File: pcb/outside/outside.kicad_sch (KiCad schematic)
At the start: 69 parts, among them J1 USB_C_Receptacle_USB2.0_16P, J2 RJ12, J3 Conn_01x08, J4 Conn_01x04, Q1 BSS138, SW1 RST, SW2 PRG, U1 ESP32-C6-MINI-1, U3 AMS1117-3.3, U4 USBLC6-2SC6, U5 USBLC6-2SC6

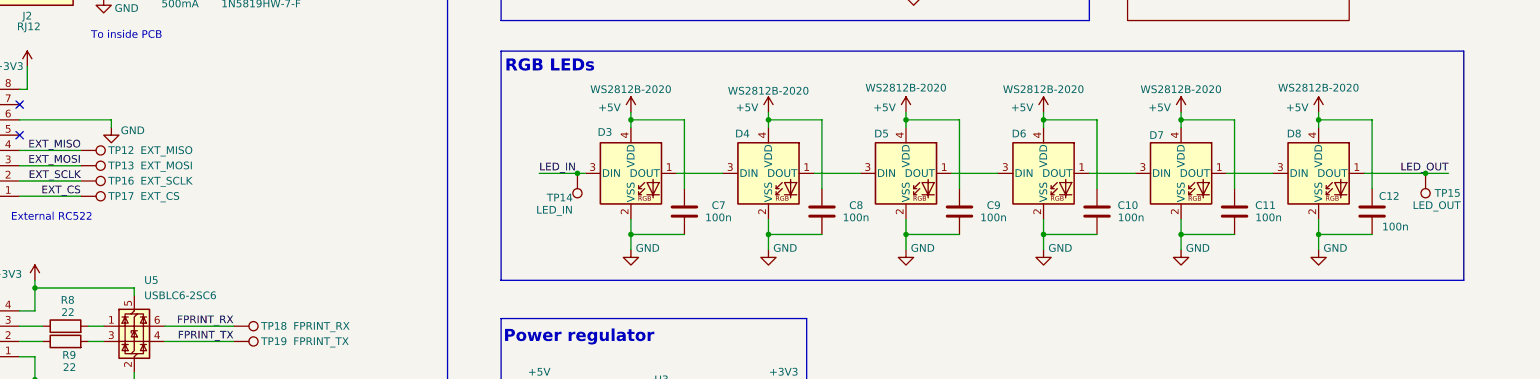
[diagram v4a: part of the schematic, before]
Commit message: fix: exclude testpoints from BOM
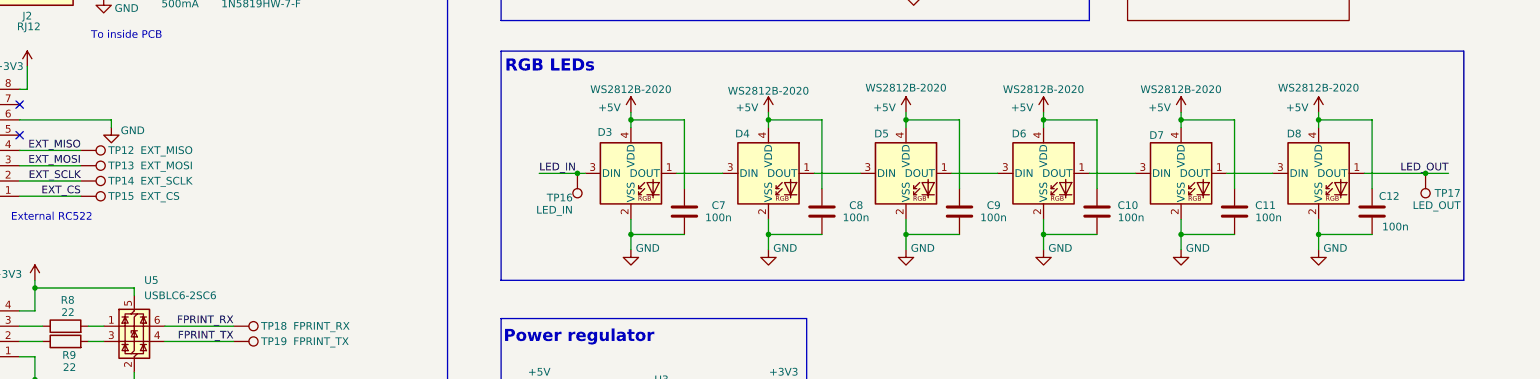
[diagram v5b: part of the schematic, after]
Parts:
- TP1, TP10, TP11, TP12, TP13, TP18, TP19, TP2, TP20, TP21, TP22, TP3, TP4, TP5, TP6, TP7, TP8, TP9: now left out of the parts list
- TP14: renamed from TP16; now left out of the parts list
- TP15: renamed from TP17; now left out of the parts list
- TP16: renamed from TP14; now left out of the parts list
- TP17: renamed from TP15; now left out of the parts list
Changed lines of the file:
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@@
 		(unit 1)
 		(exclude_from_sim no)
-		(in_bom yes)
+		(in_bom no)
 		(on_board yes)
 		(dnp no)
-		(property "Reference" "TP16"
+		(property "Reference" "TP14"
 			(at 43.942 130.81 90)
 			(effects
@@
 			(project "outside"
 				(path "/c5e20960-8abc-4599-8934-513e1dfcba6a"
-					(reference "TP16")
+					(reference "TP14")
 					(unit 1)
 				)
@@
 		(unit 1)
 		(exclude_from_sim no)
-		(in_bom yes)
+		(in_bom no)
 		(on_board yes)
 		(dnp no)
@@
 		(unit 1)
 		(exclude_from_sim no)
-		(in_bom yes)
+		(in_bom no)
 		(on_board yes)
 		(dnp no)
@@
 		(unit 1)
 		(exclude_from_sim no)
-		(in_bom yes)
+		(in_bom no)
 		(on_board yes)
 		(dnp no)
@@
 		(unit 1)
 		(exclude_from_sim no)
-		(in_bom yes)
+		(in_bom no)
 		(on_board yes)
 		(dnp no)
@@
 		(unit 1)
 		(exclude_from_sim no)
-		(in_bom yes)
+		(in_bom no)
 		(on_board yes)
 		(dnp no)
@@
 		(unit 1)
 		(exclude_from_sim no)
-		(in_bom yes)
+		(in_bom no)
 		(on_board yes)
 		(dnp no)
@@
 		(unit 1)
 		(exclude_from_sim no)
-		(in_bom yes)
+		(in_bom no)
 		(on_board yes)
 		(dnp no)
@@
 		(unit 1)
 		(exclude_from_sim no)
-		(in_bom yes)
+		(in_bom no)
 		(on_board yes)
 		(dnp no)
@@
 		(unit 1)
 		(exclude_from_sim no)
-		(in_bom yes)
+		(in_bom no)
 		(on_board yes)
 		(dnp no)
@@
 		(unit 1)
 		(exclude_from_sim no)
-		(in_bom yes)
+		(in_bom no)
 		(on_board yes)
 		(dnp no)
-		(property "Reference" "TP14"
+		(property "Reference" "TP16"
 			(at 121.158 133.604 0)
 			(effects
@@
 			(project "outside"
 				(path "/c5e20960-8abc-4599-8934-513e1dfcba6a"
-					(reference "TP14")
+					(reference "TP16")
 					(unit 1)
 				)
@@
 		(unit 1)
 		(exclude_from_sim no)
-		(in_bom yes)
+		(in_bom no)
 		(on_board yes)
 		(dnp no)
@@
 		(unit 1)
 		(exclude_from_sim no)
-		(in_bom yes)
+		(in_bom no)
 		(on_board yes)
 		(dnp no)
@@
 		(unit 1)
 		(exclude_from_sim no)
-		(in_bom yes)
+		(in_bom no)
 		(on_board yes)
 		(dnp no)
@@
 		(unit 1)
 		(exclude_from_sim no)
-		(in_bom yes)
+		(in_bom no)
 		(on_board yes)
 		(dnp no)
@@
 		(unit 1)
 		(exclude_from_sim no)
-		(in_bom yes)
+		(in_bom no)
 		(on_board yes)
 		(dnp no)
-		(property "Reference" "TP17"
+		(property "Reference" "TP15"
 			(at 43.942 133.35 90)
 			(effects
@@
 			(project "outside"
 				(path "/c5e20960-8abc-4599-8934-513e1dfcba6a"
-					(reference "TP17")
+					(reference "TP15")
 					(unit 1)
 				)
@@
 		(unit 1)
 		(exclude_from_sim no)
-		(in_bom yes)
+		(in_bom no)
 		(on_board yes)
 		(dnp no)
-		(property "Reference" "TP15"
+		(property "Reference" "TP17"
 			(at 268.732 132.842 0)
 			(effects
@@
 			(project "outside"
 				(path "/c5e20960-8abc-4599-8934-513e1dfcba6a"
-					(reference "TP15")
+					(reference "TP17")
 					(unit 1)
 				)
@@
 		(unit 1)
 		(exclude_from_sim no)
-		(in_bom yes)
+		(in_bom no)
 		(on_board yes)
 		(dnp no)
@@
 		(unit 1)
 		(exclude_from_sim no)
-		(in_bom yes)
+		(in_bom no)
 		(on_board yes)
 		(dnp no)
@@
 		(unit 1)
 		(exclude_from_sim no)
-		(in_bom yes)
+		(in_bom no)
 		(on_board yes)
 		(dnp no)
@@
 		(unit 1)
 		(exclude_from_sim no)
-		(in_bom yes)
+		(in_bom no)
 		(on_board yes)
 		(dnp no)
@@
 		(unit 1)
 		(exclude_from_sim no)
-		(in_bom yes)
+		(in_bom no)
 		(on_board yes)
 		(dnp no)

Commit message: feat: initial PCB
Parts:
- added H1, H2, H3, H4: MountingHole, MountingHole:MountingHole_3.2mm_M3, symbol Mechanical:MountingHole
